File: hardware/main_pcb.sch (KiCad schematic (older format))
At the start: 26 parts

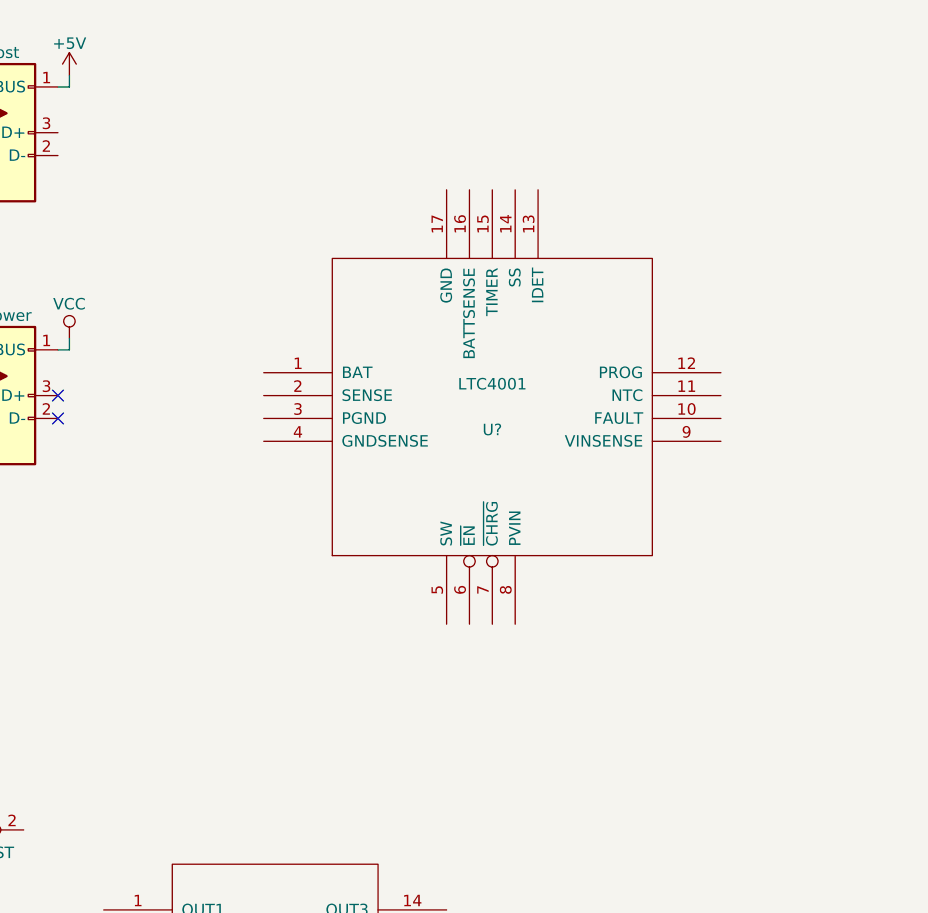
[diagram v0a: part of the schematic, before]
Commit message: schematic update
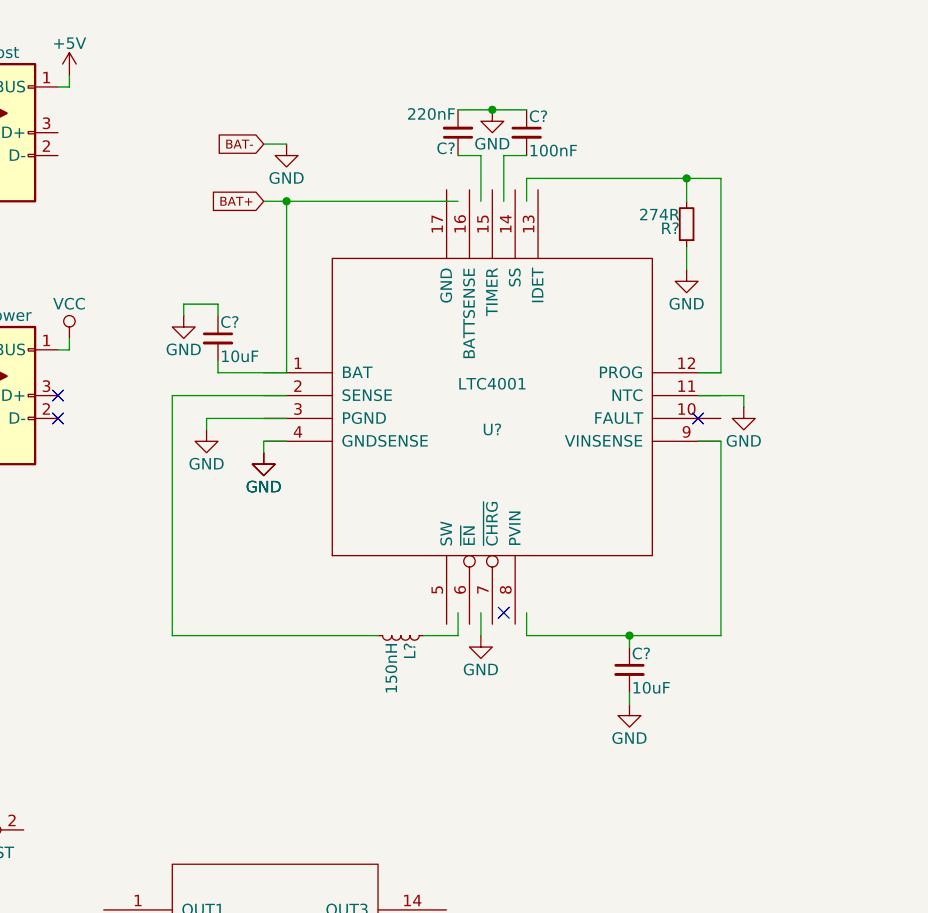
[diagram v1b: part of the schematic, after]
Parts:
- added C? (x2): 10uF, symbol C_Small
- added C?: 220nF, symbol C_Small
- added C?: 100nF, symbol C_Small
- added L?: 150nH, symbol L_Small
- added R?: 274R, symbol R_Small
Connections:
- net labels added: BAT+, BAT-
- wire segments 23 -> 60
- no-connect marks 4 -> 6

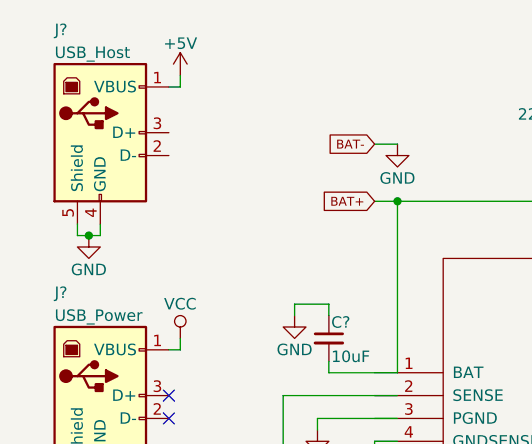
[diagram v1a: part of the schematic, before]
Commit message: swapped LTC4001
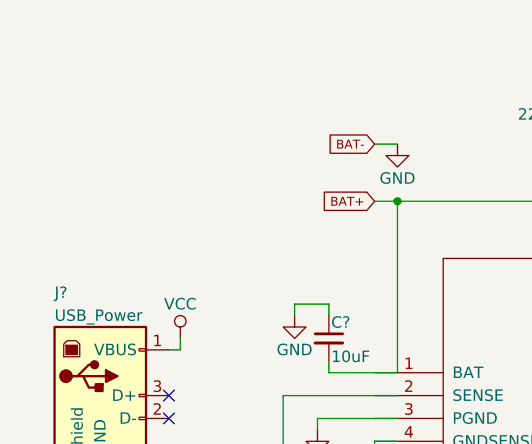
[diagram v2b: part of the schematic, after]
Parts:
- removed J?: USB_Host, symbol USB_B
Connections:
- wire segments 60 -> 55
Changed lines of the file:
@@
-$Comp
-L USB_B J?
-U 1 1 5A53DF67
-P 1000 1150
-F 0 "J?" H 800 1600 50  0000 L CNN
-F 1 "USB_Host" H 800 1500 50  0000 L CNN
-F 2 "" H 1150 1100 50  0001 C CNN
-F 3 "" H 1150 1100 50  0001 C CNN
-	1    1000 1150
-	1    0    0    -1
-$EndComp
 $Comp
 L USB_B J?
@@
 $Comp
 L GND #PWR?
-U 1 1 5A53E5F9
-P 950 1600
-F 0 "#PWR?" H 950 1350 50  0001 C CNN
-F 1 "GND" H 950 1450 50  0000 C CNN
-F 2 "" H 950 1600 50  0001 C CNN
-F 3 "" H 950 1600 50  0001 C CNN
-	1    950  1600
-	1    0    0    -1
-$EndComp
-$Comp
-L GND #PWR?
 U 1 1 5A53E61B
 P 950 2750
@@
 	1    0    0    -1
 $EndComp
-Wire Wire Line
-	1000 1600 1000 1550
-Wire Wire Line
-	900  1600 1000 1600
-Wire Wire Line
-	900  1600 900  1550
-Connection ~ 950  1600
 Wire Wire Line
 	900  2700 900  2750
@@
 $EndComp
 $Comp
-L +5V #PWR?
-U 1 1 5A553392
-P 1350 900
-F 0 "#PWR?" H 1350 750 50  0001 C CNN
-F 1 "+5V" H 1350 1040 50  0000 C CNN
-F 2 "" H 1350 900 50  0001 C CNN
-F 3 "" H 1350 900 50  0001 C CNN
-	1    1350 900
-	1    0    0    -1
-$EndComp
-Wire Wire Line
-	1350 900  1350 950
-Wire Wire Line
-	1350 950  1300 950
-$Comp
 L Conn_02x20_Odd_Even J?

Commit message: updated schematic, LTC4001 wired
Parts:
- added D?: CRG_finished, symbol LED_Small
- added D?: powered, symbol LED_Small
- added Q?: BC846, symbol Q_NPN_BCE
- added R? (x2): 470, symbol R_Small
- added R?: 1k, symbol R_Small
- added R?: 10k, symbol R_Small
- added TH?: NTC_10k, symbol Thermistor_NTC
- L?: value 150nH -> 1500nH
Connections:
- net labels added: ~CHRG
- wire segments 55 -> 75
- no-connect marks 6 -> 5
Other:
- note added: "capacitor leads should\nbe kept as short as possible\nbetween PGND and PVIN"
- note added: "low core losses"
- moved on the sheet: C?, L?

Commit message: schematic update
charging state LED inverter redone
battery state LED circuit with REF voltage
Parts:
- removed J?: AudioStereo, symbol Conn_01x03
- removed Q?: BC846, symbol Q_NPN_BCE
- removed R?: 1k, symbol R_Small
- added C? (x2): 10uF, symbol C_Small
- added D?: LED_green, symbol LED_Small
- added D? (x2): LED_yellow, symbol LED_Small
- added D?: LED_red, symbol LED_Small
- added D?: D_Small, symbol D_Small
- added J?: Headphone PJ325, symbol Audio-Jack-3_2Switches
- added J?: AudioIn, symbol Audio-Jack-3
- added J?: switchConn, symbol Conn_01x02
- added J?: LED_red_front, symbol Conn_01x02
- added R? (x13): R_Small, symbol R_Small
- added U?: LM4040C25I, symbol Shunt
- SW?: value SW_SPST -> SW_sense
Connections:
- net labels added: BAT_cmp, BAT_level_2V8, BAT_level_3V2, BAT_level_3V6, BAT_level_4V, BAT_sense, BAT_switched, Vref_1V4, Vref_1V6, Vref_1V8, Vref_2V, Vref_2V5
- wire segments 75 -> 126
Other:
- note added: "min 2V supply voltage"
- moved on the sheet: D?, J?, R?, SW?, U?

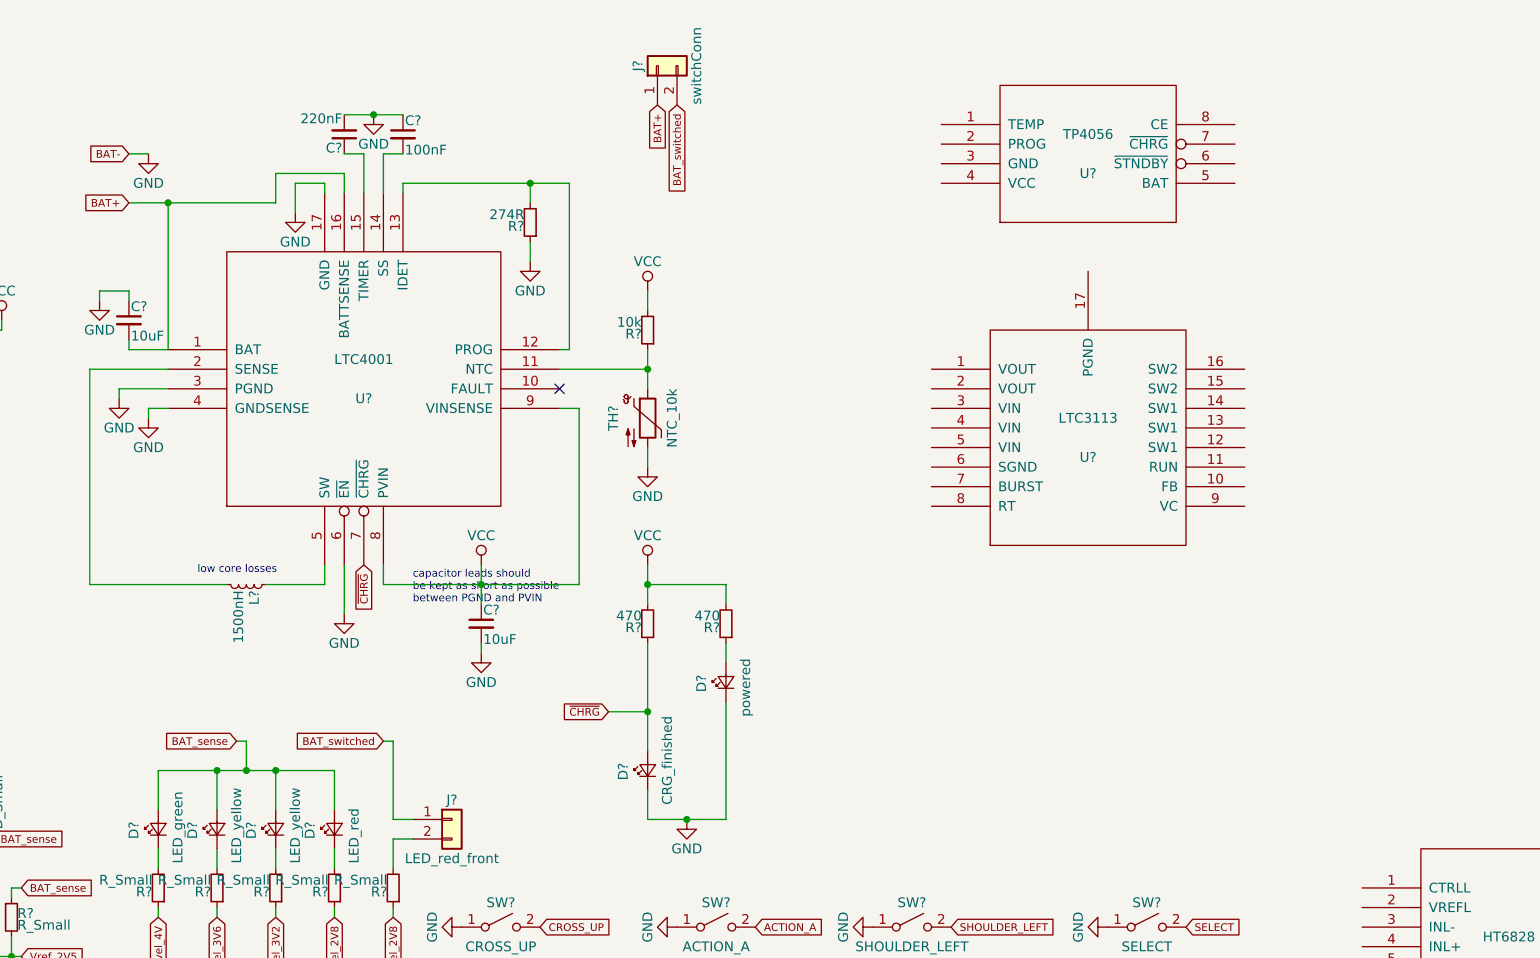
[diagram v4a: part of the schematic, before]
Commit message: pcb update
added boost to 5V
switched ltc3113 lib
changed some wiring
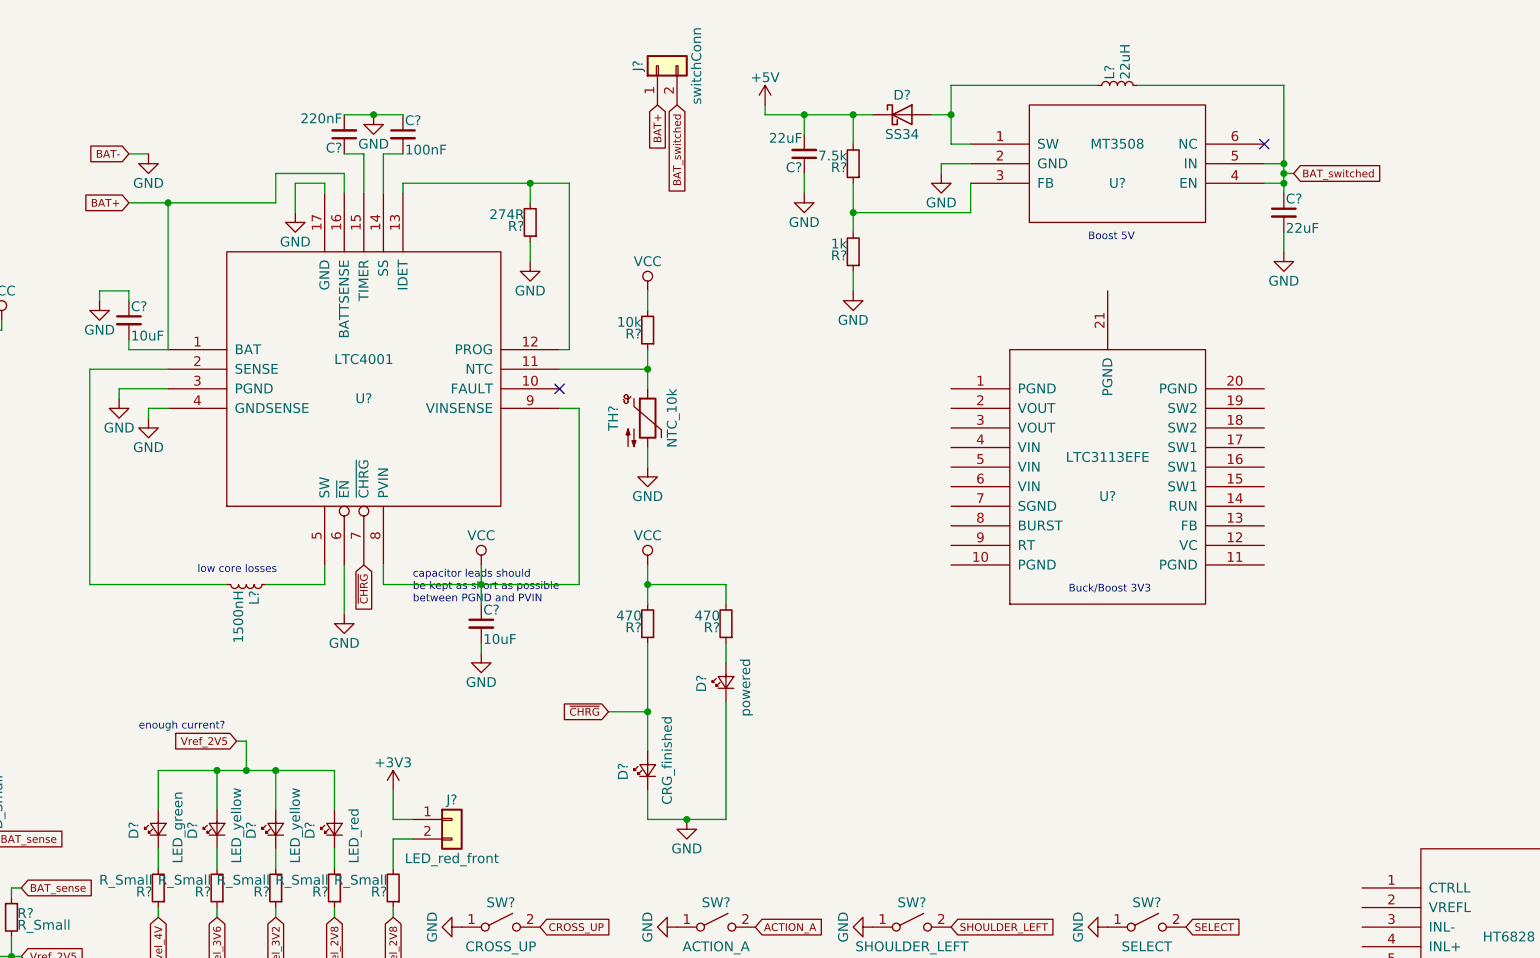
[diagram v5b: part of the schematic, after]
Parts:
- removed U?: TP4056, MODULE, symbol TP4056
- removed U?: LTC3113, MODULE, symbol LTC3113
- added C? (x2): 22uF, symbol C_Small
- added D?: SS34, symbol D_Schottky
- added L?: 22uH, symbol L_Small
- added R?: 7.5k, symbol R_Small
- added R?: 1k, symbol R_Small
- added U?: MT3508, MODULE, symbol MT3508
- added U?: LTC3113EFE, MODULE, symbol LTC3113EFE
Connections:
- net +3V3: now also J?.1 (Pin_1)
- net +5V: now also C?.2, D?.1 (K), R?.2
- net BAT_sense: no longer D?.2 (A), D?.2 (A), D?.2 (A), D?.2 (A)
- net BAT_switched: now also C?.1, L?.2, U?.4 (EN), U?.5 (IN); no longer J?.1 (Pin_1)
- net GND: now also C?.1, C?.2, R?.1, U?.2 (GND)
- net Vref_2V5: now also D?.2 (A), D?.2 (A), D?.2 (A), D?.2 (A)
- new net: D?.2 (A), L?.1, U?.1 (SW)
- new net: R?.1, R?.2, U?.3 (FB)
- no-connect marks 5 -> 6
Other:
- note added: "Boost 5V"
- note added: "Buck/Boost 3V3"
- note added: "enough current?"
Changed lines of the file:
@@
 LIBS:switches
 LIBS:shunt
+LIBS:MT3508
+LIBS:LTC3113EFE
 LIBS:main_pcb-cache
 EELAYER 25 0
@@
 $EndComp
 $Comp
-L TP4056 U?
-U 1 1 5A53E1FA
-P 6900 1200
-F 0 "U?" H 6900 1100 50  0000 C CNN
-F 1 "TP4056" H 6900 1300 50  0000 C CNN
-F 2 "MODULE" H 6900 1200 50  0001 C CNN
-F 3 "DOCUMENTATION" H 6900 1200 50  0001 C CNN
-	1    6900 1200
-	1    0    0    -1
-$EndComp
-$Comp
 L HT6828 U?
 U 1 1 5A53E325
@@
 F 3 "DOCUMENTATION" H 3300 7100 50  0001 C CNN
 	1    3300 7100
-	1    0    0    -1
-$EndComp
-$Comp
-L LTC3113 U?
-U 1 1 5A53E40B
-P 6900 2650
-F 0 "U?" H 6900 2550 50  0000 C CNN
-F 1 "LTC3113" H 6900 2750 50  0000 C CNN
-F 2 "MODULE" H 6900 2650 50  0001 C CNN
-F 3 "DOCUMENTATION" H 6900 2650 50  0001 C CNN
-	1    6900 2650
 	1    0    0    -1
 $EndComp
@@
 	-1   0    0    1
 $EndComp
-Text GLabel 2550 4200 0    39   Input ~ 0
-BAT_sense
 Text GLabel 2150 5100 3    39   Input ~ 0
 BAT_level_4V
@@
 	0    -1   -1   0
 $EndComp
-Text GLabel 3300 4200 0    39   Input ~ 0
-BAT_switched
 Wire Wire Line
 	900  2700 900  2750
@@
 Wire Wire Line
 	2550 4200 2600 4200
-Wire Wire Line
-	3300 4200 3350 4200
-Wire Wire Line
-	3350 4200 3350 4600
 $Comp
 L Conn_01x02 J?
@@
 	800  6200 800  6000
 Connection ~ 1050 6000
+$Comp
+L +3V3 #PWR?
+U 1 1 5A649081
+P 3350 4450
+F 0 "#PWR?" H 3350 4300 50  0001 C CNN
+F 1 "+3V3" H 3350 4590 50  0000 C CNN
+F 2 "" H 3350 4450 50  0001 C CNN
+F 3 "" H 3350 4450 50  0001 C CNN
+	1    3350 4450
+	1    0    0    -1
+$EndComp
+Wire Wire Line
+	3350 4450 3350 4600
+Text GLabel 2550 4200 0    39   Input ~ 0
+Vref_2V5
+Text Notes 2050 4150 0    39   ~ 0
+enough current?
+$Comp
+L MT3508 U?
+U 1 1 5A64E19D
+P 7050 1250
+F 0 "U?" H 7050 1150 50  0000 C CNN
+F 1 "MT3508" H 7050 1350 50  0000 C CNN
+F 2 "MODULE" H 7050 1250 50  0001 C CNN
+F 3 "DOCUMENTATION" H 7050 1250 50  0001 C CNN
+	1    7050 1250
+	1    0    0    -1
+$EndComp
+NoConn ~ 7800 1150
+Text GLabel 7950 1300 2    39   Input ~ 0
+BAT_switched
+Wire Wire Line
+	7900 850  7900 1400
+Wire Wire Line
+	7900 1250 7800 1250
+Wire Wire Line
+	7900 1350 7800 1350
+Wire Wire Line
+	7950 1300 7900 1300
+Connection ~ 7900 1300
+$Comp
+L GND #PWR?
+U 1 1 5A6501B2
+P 6150 1300
+F 0 "#PWR?" H 6150 1050 50  0001 C CNN
+F 1 "GND" H 6150 1150 50  0000 C CNN
+F 2 "" H 6150 1300 50  0001 C CNN
+F 3 "" H 6150 1300 50  0001 C CNN
+	1    6150 1300
+	1    0    0    -1
+$EndComp
+$Comp
+L L_Small L?
+U 1 1 5A651322
+P 7050 850
+F 0 "L?" H 7080 890 50  0000 L CNN
+F 1 "22uH" H 7080 810 50  0000 L CNN
+F 2 "" H 7050 850 50  0001 C CNN
+F 3 "" H 7050 850 50  0001 C CNN
+	1    7050 850
+	0    -1   -1   0
+$EndComp
+Wire Wire Line
+	7150 850  7900 850
+Connection ~ 7900 1250
+Wire Wire Line
+	6950 850  6200 850
+Wire Wire Line
+	6200 850  6200 1150
+Wire Wire Line
+	6200 1150 6300 1150
+$Comp
+L C_Small C?
+U 1 1 5A652B0C
+P 7900 1500
+F 0 "C?" H 7910 1570 50  0000 L CNN
+F 1 "22uF" H 7910 1420 50  0000 L CNN
+F 2 "" H 7900 1500 50  0001 C CNN
+F 3 "" H 7900 1500 50  0001 C CNN
+	1    7900 1500
+	1    0    0    -1
+$EndComp
+Connection ~ 7900 1350
+$Comp
+L GND #PWR?
+U 1 1 5A653AB3
+P 7900 1700
+F 0 "#PWR?" H 7900 1450 50  0001 C CNN
+F 1 "GND" H 7900 1550 50  0000 C CNN
+F 2 "" H 7900 1700 50  0001 C CNN
+F 3 "" H 7900 1700 50  0001 C CNN
+	1    7900 1700
+	1    0    0    -1
+$EndComp
+Wire Wire Line
+	7900 1700 7900 1600
+Wire Wire Line
+	6150 1300 6150 1250
+Wire Wire Line
+	6150 1250 6300 1250
+$Comp
+L D_Schottky D?
+U 1 1 5A656372
+P 5950 1000
+F 0 "D?" H 5950 1100 50  0000 C CNN
+F 1 "SS34" H 5950 900 50  0000 C CNN
+F 2 "" H 5950 1000 50  0001 C CNN
+F 3 "" H 5950 1000 50  0001 C CNN
+	1    5950 1000
+	1    0    0    -1
+$EndComp
+Wire Wire Line
+	6100 1000 6200 1000
+Connection ~ 6200 1000
+Wire Wire Line
+	6300 1350 6300 1500
+Wire Wire Line
+	6300 1500 5700 1500
+$Comp
+L R_Small R?
+U 1 1 5A658818
+P 5700 1250
+F 0 "R?" H 5730 1270 50  0000 L CNN
+F 1 "7.5k" H 5730 1210 50  0000 L CNN
+F 2 "" H 5700 1250 50  0001 C CNN
+F 3 "" H 5700 1250 50  0001 C CNN
+	1    5700 1250
+	-1   0    0    1
+$EndComp
+$Comp
+L R_Small R?
+U 1 1 5A65892B
+P 5700 1700
+F 0 "R?" H 5730 1720 50  0000 L CNN
+F 1 "1k" H 5730 1660 50  0000 L CNN
+F 2 "" H 5700 1700 50  0001 C CNN
+F 3 "" H 5700 1700 50  0001 C CNN
+	1    5700 1700
+	-1   0    0    1
+$EndComp
+$Comp
+L GND #PWR?
+U 1 1 5A658A13
+P 5700 1900
+F 0 "#PWR?" H 5700 1650 50  0001 C CNN
+F 1 "GND" H 5700 1750 50  0000 C CNN
+F 2 "" H 5700 1900 50  0001 C CNN
+F 3 "" H 5700 1900 50  0001 C CNN
+	1    5700 1900
+	1    0    0    -1
+$EndComp
+Wire Wire Line
+	5700 1900 5700 1800
+Wire Wire Line
+	5700 1350 5700 1600
+Connection ~ 5700 1500
+Wire Wire Line
+	5700 1150 5700 1000
+Wire Wire Line
+	5250 1000 5800 1000
+Connection ~ 5700 1000
+$Comp
+L C_Small C?
+U 1 1 5A65C0C4
+P 5450 1200
+F 0 "C?" H 5460 1270 50  0000 L CNN
+F 1 "22uF" H 5460 1120 50  0000 L CNN
+F 2 "" H 5450 1200 50  0001 C CNN
+F 3 "" H 5450 1200 50  0001 C CNN
+	1    5450 1200
+	-1   0    0    1
+$EndComp
+$Comp
+L GND #PWR?
+U 1 1 5A65C1E1
+P 5450 1400
+F 0 "#PWR?" H 5450 1150 50  0001 C CNN
+F 1 "GND" H 5450 1250 50  0000 C CNN
+F 2 "" H 5450 1400 50  0001 C CNN
+F 3 "" H 5450 1400 50  0001 C CNN
+	1    5450 1400
+	1    0    0    -1
+$EndComp
+Wire Wire Line
+	5450 1400 5450 1300
+Wire Wire Line
+	5450 1100 5450 1000
+Connection ~ 5450 1000
+$Comp
+L +5V #PWR?
+U 1 1 5A65CB6B
+P 5250 950
+F 0 "#PWR?" H 5250 800 50  0001 C CNN
+F 1 "+5V" H 5250 1090 50  0000 C CNN
+F 2 "" H 5250 950 50  0001 C CNN
+F 3 "" H 5250 950 50  0001 C CNN
+	1    5250 950
+	1    0    0    -1
+$EndComp
+Wire Wire Line
+	5250 950  5250 1000
+Text Notes 6900 1650 0    39   ~ 0
+Boost 5V
+Text Notes 6800 3450 0    39   ~ 0
+Buck/Boost 3V3
+$Comp
+L LTC3113EFE U?
+U 1 1 5A667351
+P 7000 2850
+F 0 "U?" H 7000 2750 50  0000 C CNN
+F 1 "LTC3113EFE" H 7000 2950 50  0000 C CNN
+F 2 "MODULE" H 7000 2850 50  0001 C CNN
+F 3 "DOCUMENTATION" H 7000 2850 50  0001 C CNN
+	1    7000 2850
+	1    0    0    -1
+$EndComp
 $EndSCHEMATC
